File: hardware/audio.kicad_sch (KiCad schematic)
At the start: 0 parts

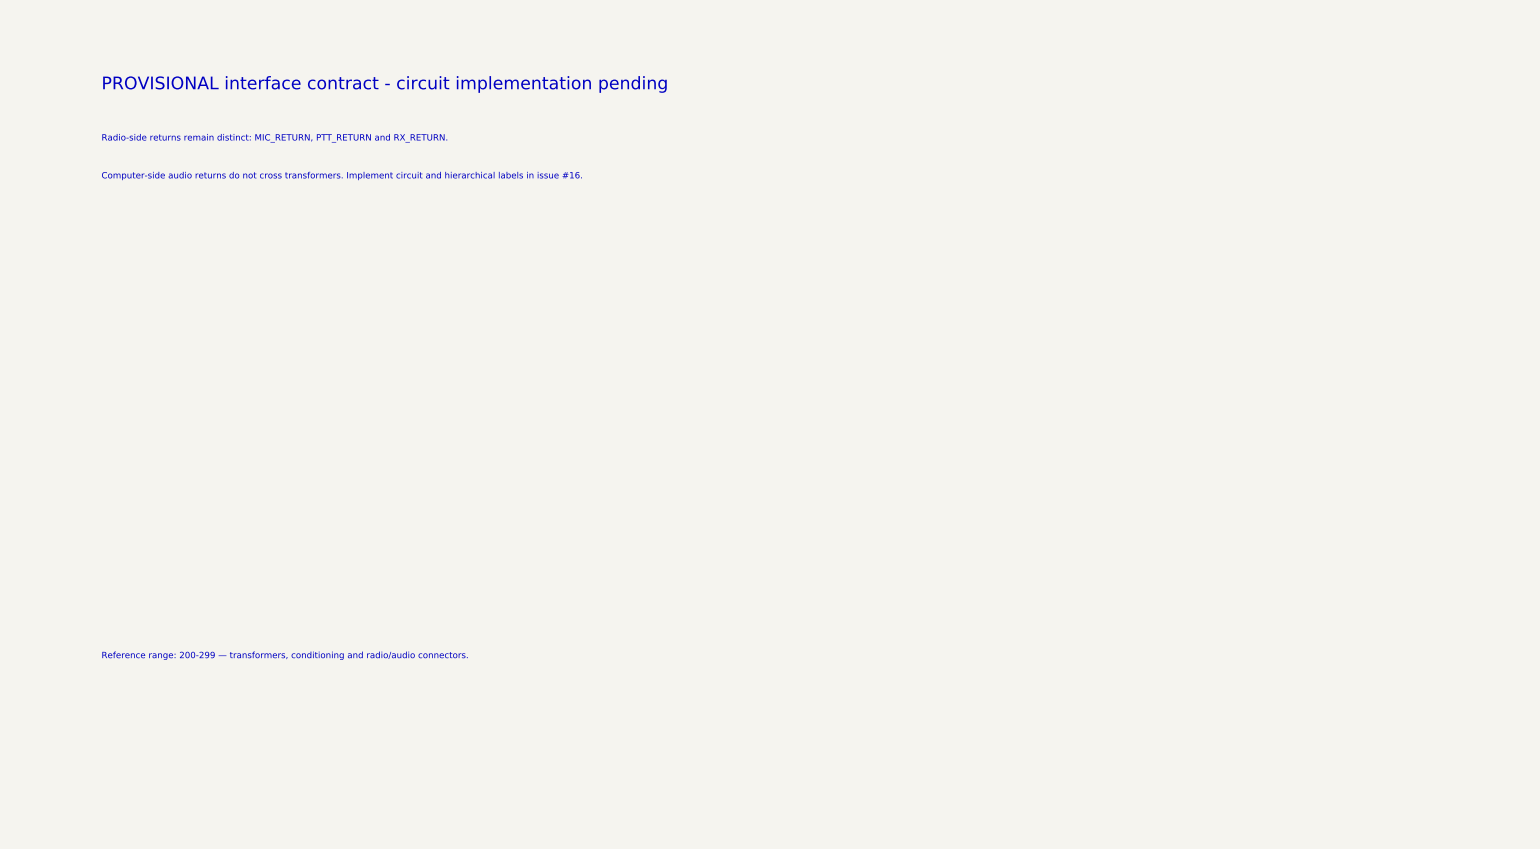
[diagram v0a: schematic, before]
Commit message: cad: add provisional isolated audio architecture
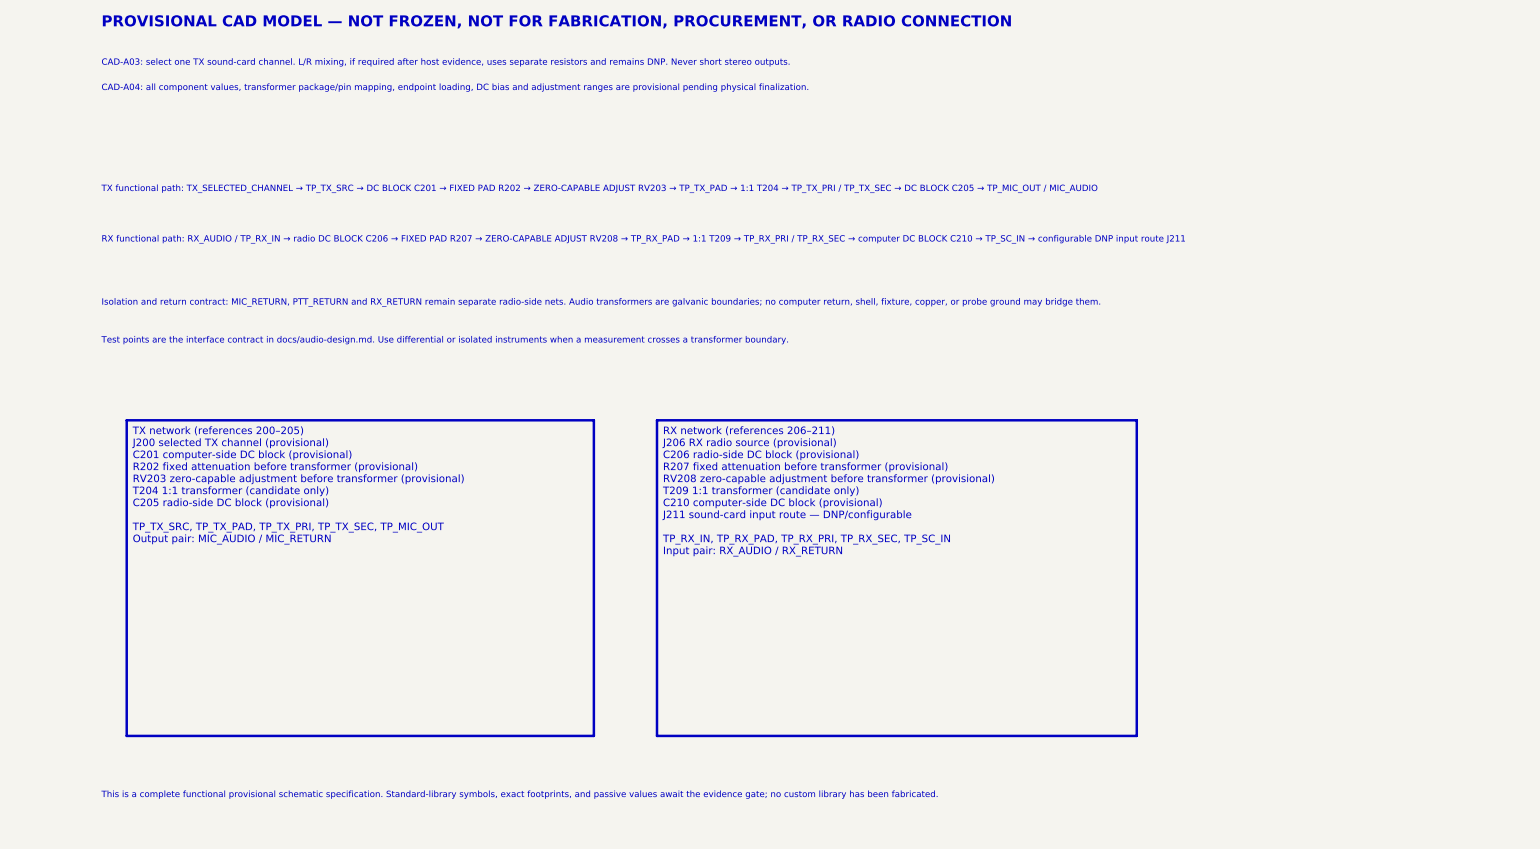
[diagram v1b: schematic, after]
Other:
- note added: "CAD-A03: select one TX sound-card channel. L/R mixing, if required after host evidence, uses separate resistors and remains DNP. Never short stereo outputs."
- note added: "CAD-A04: all component values, transformer package/pin mapping, endpoint loading, DC bias and adjustment ranges are provisional pending physical finalization."
- note added: "Isolation and return contract: MIC_RETURN, PTT_RETURN and RX_RETURN remain separate radio-side nets. Audio transformers are galvanic boundaries; no computer return, shell, fixture, copper, or probe ground may bridge them."
- note added: "PROVISIONAL CAD MODEL — NOT FROZEN, NOT FOR FABRICATION, PROCUREMENT, OR RADIO CONNECTION"
- note added: "RX functional path: RX_AUDIO / TP_RX_IN → radio DC BLOCK C206 → FIXED PAD R207 → ZERO-CAPABLE ADJUST RV208 → TP_RX_PAD → 1:1 T209 → TP_RX_PRI / TP_RX_SEC → computer DC BLOCK C210 → TP_SC_IN → configurable DNP input route J211"
- note added: "TX functional path: TX_SELECTED_CHANNEL → TP_TX_SRC → DC BLOCK C201 → FIXED PAD R202 → ZERO-CAPABLE ADJUST RV203 → TP_TX_PAD → 1:1 T204 → TP_TX_PRI / TP_TX_SEC → DC BLOCK C205 → TP_MIC_OUT / MIC_AUDIO"
- note added: "Test points are the interface contract in docs/audio-design.md. Use differential or isolated instruments when a measurement crosses a transformer boundary."
- note added: "This is a complete functional provisional schematic specification. Standard-library symbols, exact footprints, and passive values await the evidence gate; no custom library has been fabricated."
- note removed: "Computer-side audio returns do not cross transformers. Implement circuit and hierarchical labels in issue #16."
- note removed: "PROVISIONAL interface contract - circuit implementation pending"
- note removed: "Radio-side returns remain distinct: MIC_RETURN, PTT_RETURN and RX_RETURN."
- note removed: "Reference range: 200-299 — transformers, conditioning and radio/audio connectors."
- title: Transformer-coupled TX and RX audio -> Transformer-coupled TX and RX audio — PROVISIONAL
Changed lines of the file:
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@@
 	(generator "eeschema")
 	(paper "A4")
-	(title_block
-		(title "Transformer-coupled TX and RX audio")
-		(rev "A-PROVISIONAL")
-		(comment 1 "NOT FROZEN - NOT FOR FABRICATION")
-	)
-	(text "PROVISIONAL interface contract - circuit implementation pending"
-		(at 25.4 30.48 0)
-		(effects (font (size 2.54 2.54)) (justify left bottom))
-	)
-	(text "Radio-side returns remain distinct: MIC_RETURN, PTT_RETURN and RX_RETURN."
-		(at 25.4 40.64 0)
-		(effects (font (size 1.27 1.27)) (justify left bottom))
-	)
-	(text "Computer-side audio returns do not cross transformers. Implement circuit and hierarchical labels in issue #16."
-		(at 25.4 48.26 0)
-		(effects (font (size 1.27 1.27)) (justify left bottom))
-	)
-	(text "Reference range: 200-299 — transformers, conditioning and radio/audio connectors."
-		(at 25.4 144.78 0)
-		(effects (font (size 1.27 1.27)) (justify left bottom))
-	)
+	(title_block (title "Transformer-coupled TX and RX audio — PROVISIONAL") (rev "A-PROVISIONAL") (comment 1 "NOT FROZEN — NOT FOR FABRICATION OR PROCUREMENT") (comment 2 "CAD-A03 / CAD-A04 require physical finalization"))
+	(text "PROVISIONAL CAD MODEL — NOT FROZEN, NOT FOR FABRICATION, PROCUREMENT, OR RADIO CONNECTION"
+		(at 25.4 17.78 0) (effects (font (size 2.2 2.2) (bold yes)) (justify left bottom)))
+	(text "CAD-A03: select one TX sound-card channel. L/R mixing, if required after host evidence, uses separate resistors and remains DNP. Never short stereo outputs."
+		(at 25.4 25.4 0) (effects (font (size 1.27 1.27)) (justify left bottom)))
+	(text "CAD-A04: all component values, transformer package/pin mapping, endpoint loading, DC bias and adjustment ranges are provisional pending physical finalization."
+		(at 25.4 30.48 0) (effects (font (size 1.27 1.27)) (justify left bottom)))
+	(text "TX functional path: TX_SELECTED_CHANNEL → TP_TX_SRC → DC BLOCK C201 → FIXED PAD R202 → ZERO-CAPABLE ADJUST RV203 → TP_TX_PAD → 1:1 T204 → TP_TX_PRI / TP_TX_SEC → DC BLOCK C205 → TP_MIC_OUT / MIC_AUDIO"
+		(at 25.4 50.8 0) (effects (font (size 1.27 1.27)) (justify left bottom)))
+	(text "RX functional path: RX_AUDIO / TP_RX_IN → radio DC BLOCK C206 → FIXED PAD R207 → ZERO-CAPABLE ADJUST RV208 → TP_RX_PAD → 1:1 T209 → TP_RX_PRI / TP_RX_SEC → computer DC BLOCK C210 → TP_SC_IN → configurable DNP input route J211"
+		(at 25.4 60.96 0) (effects (font (size 1.27 1.27)) (justify left bottom)))
+	(text "Isolation and return contract: MIC_RETURN, PTT_RETURN and RX_RETURN remain separate radio-side nets. Audio transformers are galvanic boundaries; no computer return, shell, fixture, copper, or probe ground may bridge them."
+		(at 25.4 73.66 0) (effects (font (size 1.27 1.27)) (justify left bottom)))
+	(text "Test points are the interface contract in docs/audio-design.md. Use differential or isolated instruments when a measurement crosses a transformer boundary."
+		(at 25.4 81.28 0) (effects (font (size 1.27 1.27)) (justify left bottom)))
+	(text_box "TX network (references 200–205)\nJ200 selected TX channel (provisional)\nC201 computer-side DC block (provisional)\nR202 fixed attenuation before transformer (provisional)\nRV203 zero-capable adjustment before transformer (provisional)\nT204 1:1 transformer (candidate only)\nC205 radio-side DC block (provisional)\n\nTP_TX_SRC, TP_TX_PAD, TP_TX_PRI, TP_TX_SEC, TP_MIC_OUT\nOutput pair: MIC_AUDIO / MIC_RETURN"
+		(exclude_from_sim no) (at 30.48 96.52 0) (size 93.98 63.5) (stroke (width 0.5) (type default)) (fill (type background))
+		(effects (font (size 1.5 1.5)) (justify left top)))
+	(text_box "RX network (references 206–211)\nJ206 RX radio source (provisional)\nC206 radio-side DC block (provisional)\nR207 fixed attenuation before transformer (provisional)\nRV208 zero-capable adjustment before transformer (provisional)\nT209 1:1 transformer (candidate only)\nC210 computer-side DC block (provisional)\nJ211 sound-card input route — DNP/configurable\n\nTP_RX_IN, TP_RX_PAD, TP_RX_PRI, TP_RX_SEC, TP_SC_IN\nInput pair: RX_AUDIO / RX_RETURN"
+		(exclude_from_sim no) (at 137.16 96.52 0) (size 96.52 63.5) (stroke (width 0.5) (type default)) (fill (type background))
+		(effects (font (size 1.5 1.5)) (justify left top)))
+	(text "This is a complete functional provisional schematic specification. Standard-library symbols, exact footprints, and passive values await the evidence gate; no custom library has been fabricated."
+		(at 25.4 172.72 0) (effects (font (size 1.27 1.27)) (justify left bottom)))
+	(sheet_instances (path "/" (page "1")))
 	(embedded_fonts no)
 )

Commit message: cad: wire provisional audio paths
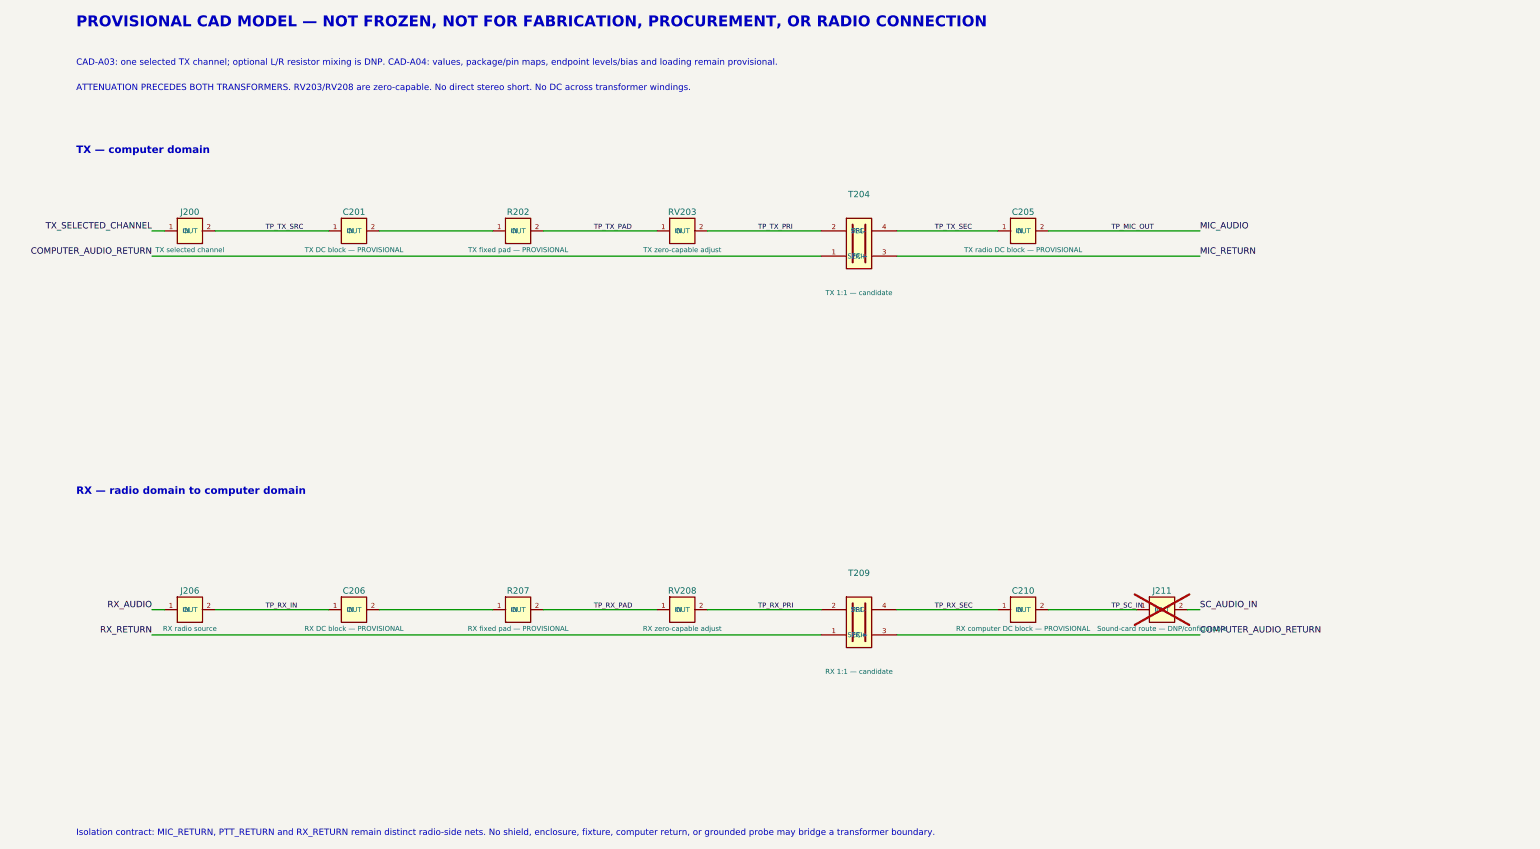
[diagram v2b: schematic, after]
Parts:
- added C201: TX DC block — PROVISIONAL, symbol TS700:Audio2
- added C205: TX radio DC block — PROVISIONAL, symbol TS700:Audio2
- added C206: RX DC block — PROVISIONAL, symbol TS700:Audio2
- added C210: RX computer DC block — PROVISIONAL, symbol TS700:Audio2
- added J200: TX selected channel, symbol TS700:Audio2
- added J206: RX radio source, symbol TS700:Audio2
- added J211: Sound-card route — DNP/configurable, symbol TS700:Audio2
- added R202: TX fixed pad — PROVISIONAL, symbol TS700:Audio2
- added R207: RX fixed pad — PROVISIONAL, symbol TS700:Audio2
- added RV203: TX zero-capable adjust, symbol TS700:Audio2
- added RV208: RX zero-capable adjust, symbol TS700:Audio2
- added T204: TX 1:1 — candidate, symbol TS700:Transformer1to1
- added T209: RX 1:1 — candidate, symbol TS700:Transformer1to1
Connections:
- new net: C201.2 (OUT), R202.1 (IN)
- new net: C206.2 (OUT), R207.1 (IN)
- new net COMPUTER_AUDIO_RETURN: T204.1 (PRI+), T209.3 (SEC+)
- new net MIC_AUDIO: C205.2 (OUT)
- new net MIC_RETURN: T204.3 (SEC+)
- new net RX_AUDIO: J206.1 (IN)
- new net RX_RETURN: T209.1 (PRI+)
- new net SC_AUDIO_IN: J211.2 (OUT)
- new net TP_RX_IN: C206.1 (IN), J206.2 (OUT)
- new net TP_RX_PAD: R207.2 (OUT), RV208.1 (IN)
- new net TP_RX_PRI: RV208.2 (OUT), T209.2 (PRI-)
- new net TP_RX_SEC: C210.1 (IN), T209.4 (SEC-)
- new net TP_SC_IN: C210.2 (OUT), J211.1 (IN)
- new net TP_TX_PAD: R202.2 (OUT), RV203.1 (IN)
- new net TP_TX_PRI: RV203.2 (OUT), T204.2 (PRI-)
- new net TP_TX_SEC: C205.1 (IN), T204.4 (SEC-)
- new net TP_TX_SRC: C201.1 (IN), J200.2 (OUT)
- new net TX_SELECTED_CHANNEL: J200.1 (IN)
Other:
- note added: "ATTENUATION PRECEDES BOTH TRANSFORMERS. RV203/RV208 are zero-capable. No direct stereo short. No DC across transformer windings."
- note added: "CAD-A03: one selected TX channel; optional L/R resistor mixing is DNP. CAD-A04: values, package/pin maps, endpoint levels/bias and loading remain provisional."
- note added: "Isolation contract: MIC_RETURN, PTT_RETURN and RX_RETURN remain distinct radio-side nets. No shield, enclosure, fixture, computer return, or grounded probe may bridge a transformer boundary."
- note added: "RX — radio domain to computer domain"
- note added: "TX — computer domain"
- note removed: "CAD-A03: select one TX sound-card channel. L/R mixing, if required after host evidence, uses separate resistors and remains DNP. Never short stereo outputs."
- note removed: "CAD-A04: all component values, transformer package/pin mapping, endpoint loading, DC bias and adjustment ranges are provisional pending physical finalization."
- note removed: "Isolation and return contract: MIC_RETURN, PTT_RETURN and RX_RETURN remain separate radio-side nets. Audio transformers are galvanic boundaries; no computer return, shell, fixture, copper, or probe ground may bridge them."
- note removed: "RX functional path: RX_AUDIO / TP_RX_IN → radio DC BLOCK C206 → FIXED PAD R207 → ZERO-CAPABLE ADJUST RV208 → TP_RX_PAD → 1:1 T209 → TP_RX_PRI / TP_RX_SEC → computer DC BLOCK C210 → TP_SC_IN → configurable DNP input route J211"
- note removed: "TX functional path: TX_SELECTED_CHANNEL → TP_TX_SRC → DC BLOCK C201 → FIXED PAD R202 → ZERO-CAPABLE ADJUST RV203 → TP_TX_PAD → 1:1 T204 → TP_TX_PRI / TP_TX_SEC → DC BLOCK C205 → TP_MIC_OUT / MIC_AUDIO"
- note removed: "Test points are the interface contract in docs/audio-design.md. Use differential or isolated instruments when a measurement crosses a transformer boundary."
- note removed: "This is a complete functional provisional schematic specification. Standard-library symbols, exact footprints, and passive values await the evidence gate; no custom library has been fabricated."
- title: Transformer-coupled TX and RX audio — PROVISIONAL -> TS-700SP isolated TX/RX audio — PROVISIONAL
